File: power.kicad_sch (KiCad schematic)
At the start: 72 parts, among them Q2 PJE138K, Q3 PJE138K, U27 AP62301_TSOT, U28 AP62301_TSOT, U29 SIC431AED-T1-GE3, U30 TPS22976DPUR, U31 TPS22976DPUR

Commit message: [#83736] WIP: Clear ERC
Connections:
- net VCC is gone; now on net +12V_IN: R249.2
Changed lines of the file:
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@@
 	)
 	(junction
+		(at 62.23 72.39)
+		(diameter 0)
+		(color 0 0 0 0)
+	)
+	(junction
 		(at 189.23 77.47)
 		(diameter 0)
@@
 	(wire
 		(pts
-			(xy 59.69 72.39) (xy 104.14 72.39)
+			(xy 59.69 72.39) (xy 62.23 72.39)
 		)
 		(stroke
@@
 	(wire
 		(pts
+			(xy 76.2 48.26) (xy 62.23 48.26)
+		)
+		(stroke
+			(width 0)
+			(type default)
+		)
+	)
+	(wire
+		(pts
 			(xy 165.1 172.72) (xy 165.1 177.8)
 		)
@@
 	(wire
 		(pts
+			(xy 62.23 48.26) (xy 62.23 72.39)
+		)
+		(stroke
+			(width 0)
+			(type default)
+		)
+	)
+	(wire
+		(pts
 			(xy 378.46 200.66) (xy 381 200.66)
 		)
@@
 	(wire
 		(pts
+			(xy 62.23 72.39) (xy 104.14 72.39)
+		)
+		(stroke
+			(width 0)
+			(type default)
+		)
+	)
+	(wire
+		(pts
 			(xy 124.46 238.76) (xy 129.54 238.76)
 		)
@@
 					(unit 1)
 				)
-			)
-		)
-	)
-	(symbol
-		(lib_id "antmicropower:VCC")
-		(at 76.2 48.26 0)
-		(unit 1)
-		(exclude_from_sim no)
-		(in_bom yes)
-		(on_board yes)
-		(dnp no)
-		(property "Reference" "#PWR0255"
-			(at 76.2 52.07 0)
-			(effects
-				(font
-					(size 1.27 1.27)
-				)
-				(justify left bottom)
-				(hide yes)
-			)
-		)
-		(property "Value" "VCC"
-			(at 74.295 44.45 0)
-			(effects
-				(font
-					(size 1.27 1.27)
-				)
-				(justify left)
-			)
-		)
-		(property "Footprint" ""
-			(at 76.2 48.26 0)
-			(effects
-				(font
-					(size 1.27 1.27)
-				)
-				(hide yes)
-			)
-		)
-		(property "Datasheet" ""
-			(at 76.2 48.26 0)
-			(effects
-				(font
-					(size 1.27 1.27)
-				)
-				(hide yes)
-			)
-		)
-		(property "Description" ""
-			(at 76.2 48.26 0)
-			(effects
-				(font
-					(size 1.27 1.27)
-				)
-				(hide yes)
-			)
-		)
-		(pin "1"
-		)
-		(instances
-			(project "bmc-reference-carrier-board"
-				(path "/5f636c45-3c15-4731-8931-4625e0dab7e4/3d29c412-58cb-45c0-928a-e05b1352002d"
-					(reference "#PWR0255")
-					(unit 1)
-				)

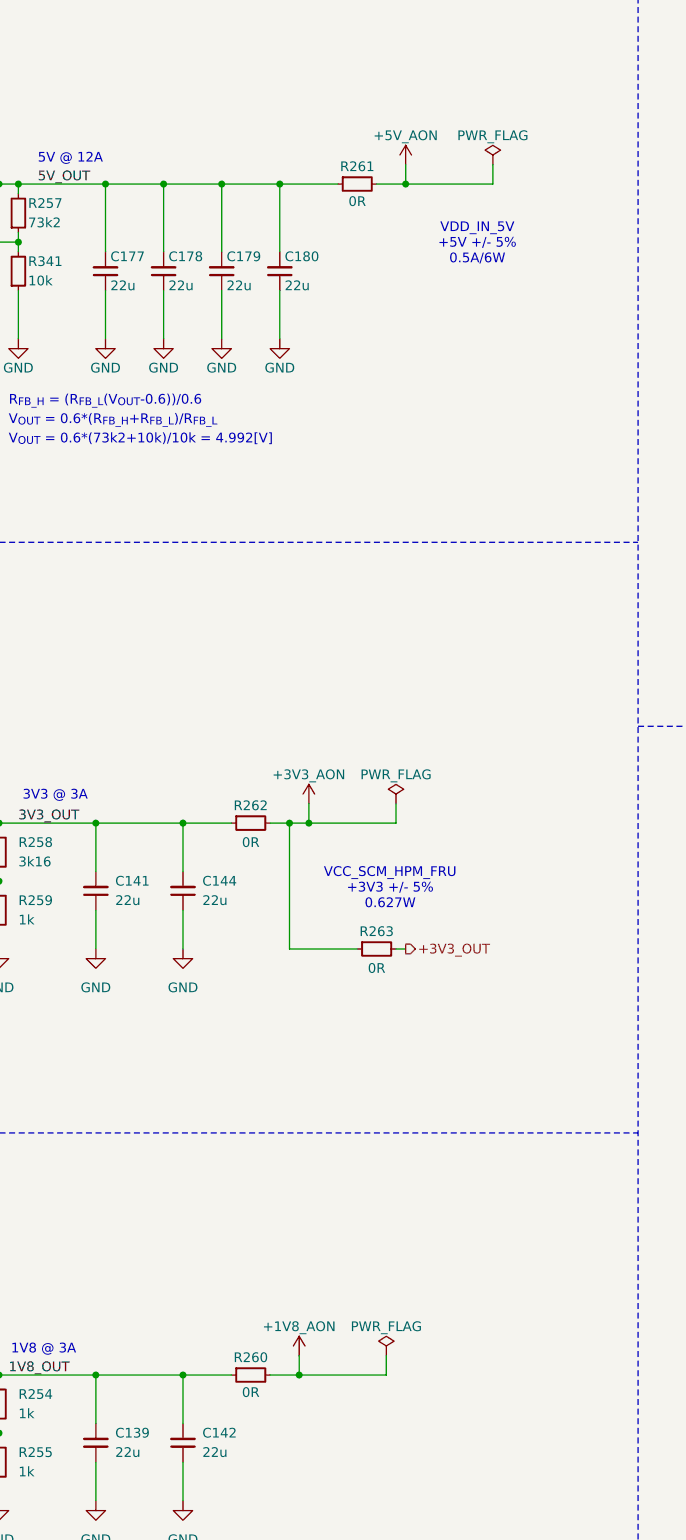
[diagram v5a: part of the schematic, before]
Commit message: [#83767] Layout DC-DC converters, change 0R on power rails to one that can handle more current
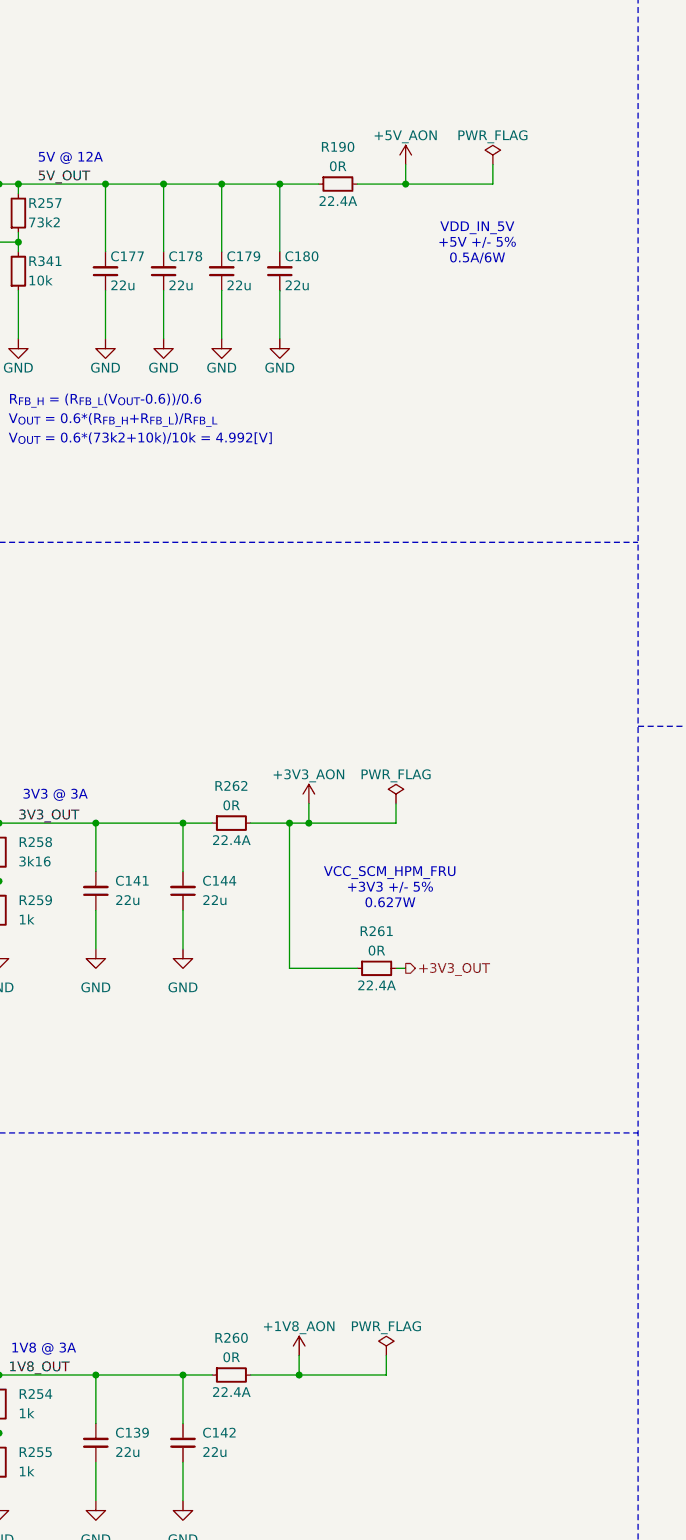
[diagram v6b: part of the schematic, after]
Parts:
- removed R260, R261, R262, R263: R_0R_0402, antmicro-footprints:R_0402_1005Metric, symbol antmicroResistors0402:R_0R_0402
- added R190, R260, R261, R262: R_0R_22.4A_0603, antmicro-footprints:R_0603_1608Metric, symbol antmicroResistors0603:R_0R_22.4A_0603
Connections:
- net +1V8_AON: now also R260.2
- net +3V3_AON: now also R261.1, R262.2
- net +3V3_OUT: now also R261.2
- net +5V_AON: now also R190.2
- net 1V8_OUT: now also R260.1
- net 3V3_OUT: now also R262.1
- net 5V_OUT: now also R190.1

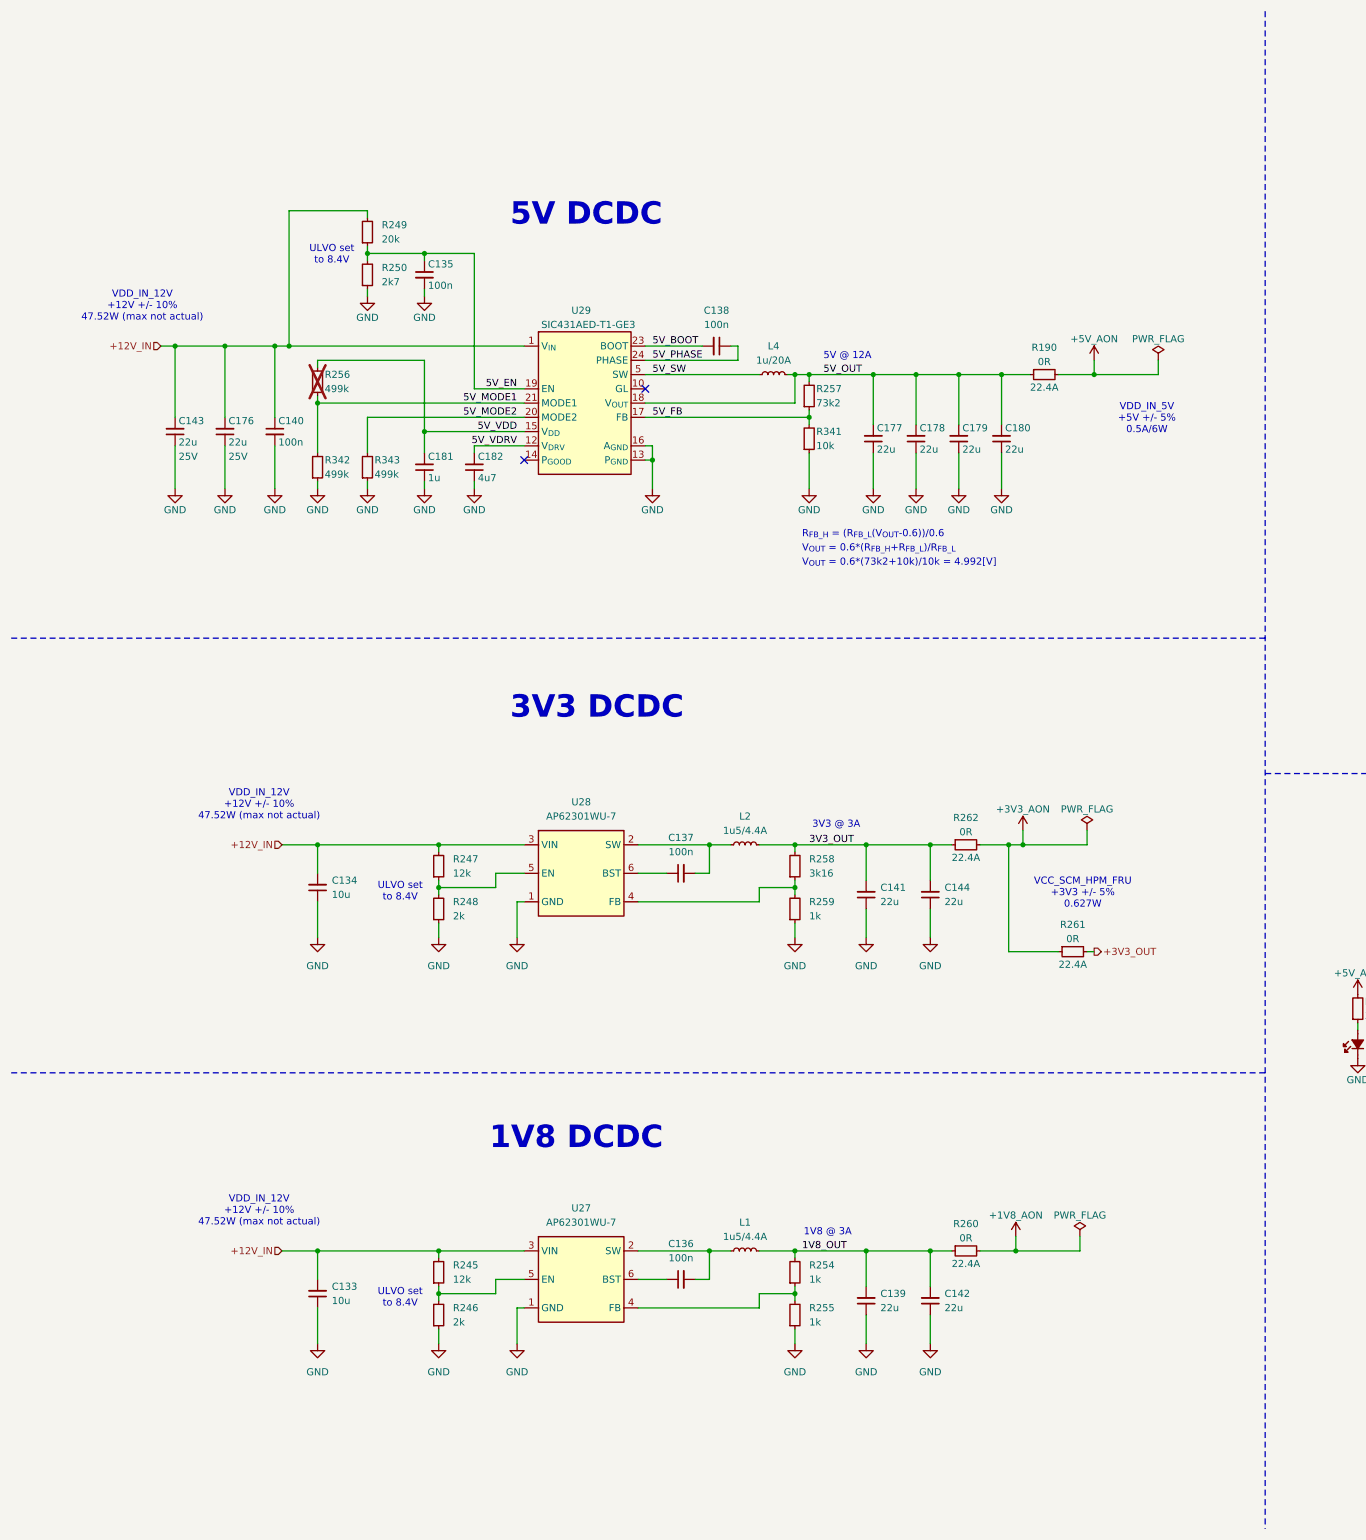
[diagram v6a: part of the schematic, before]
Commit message: [#83904] Add current monitoring IC to the 12V input rail
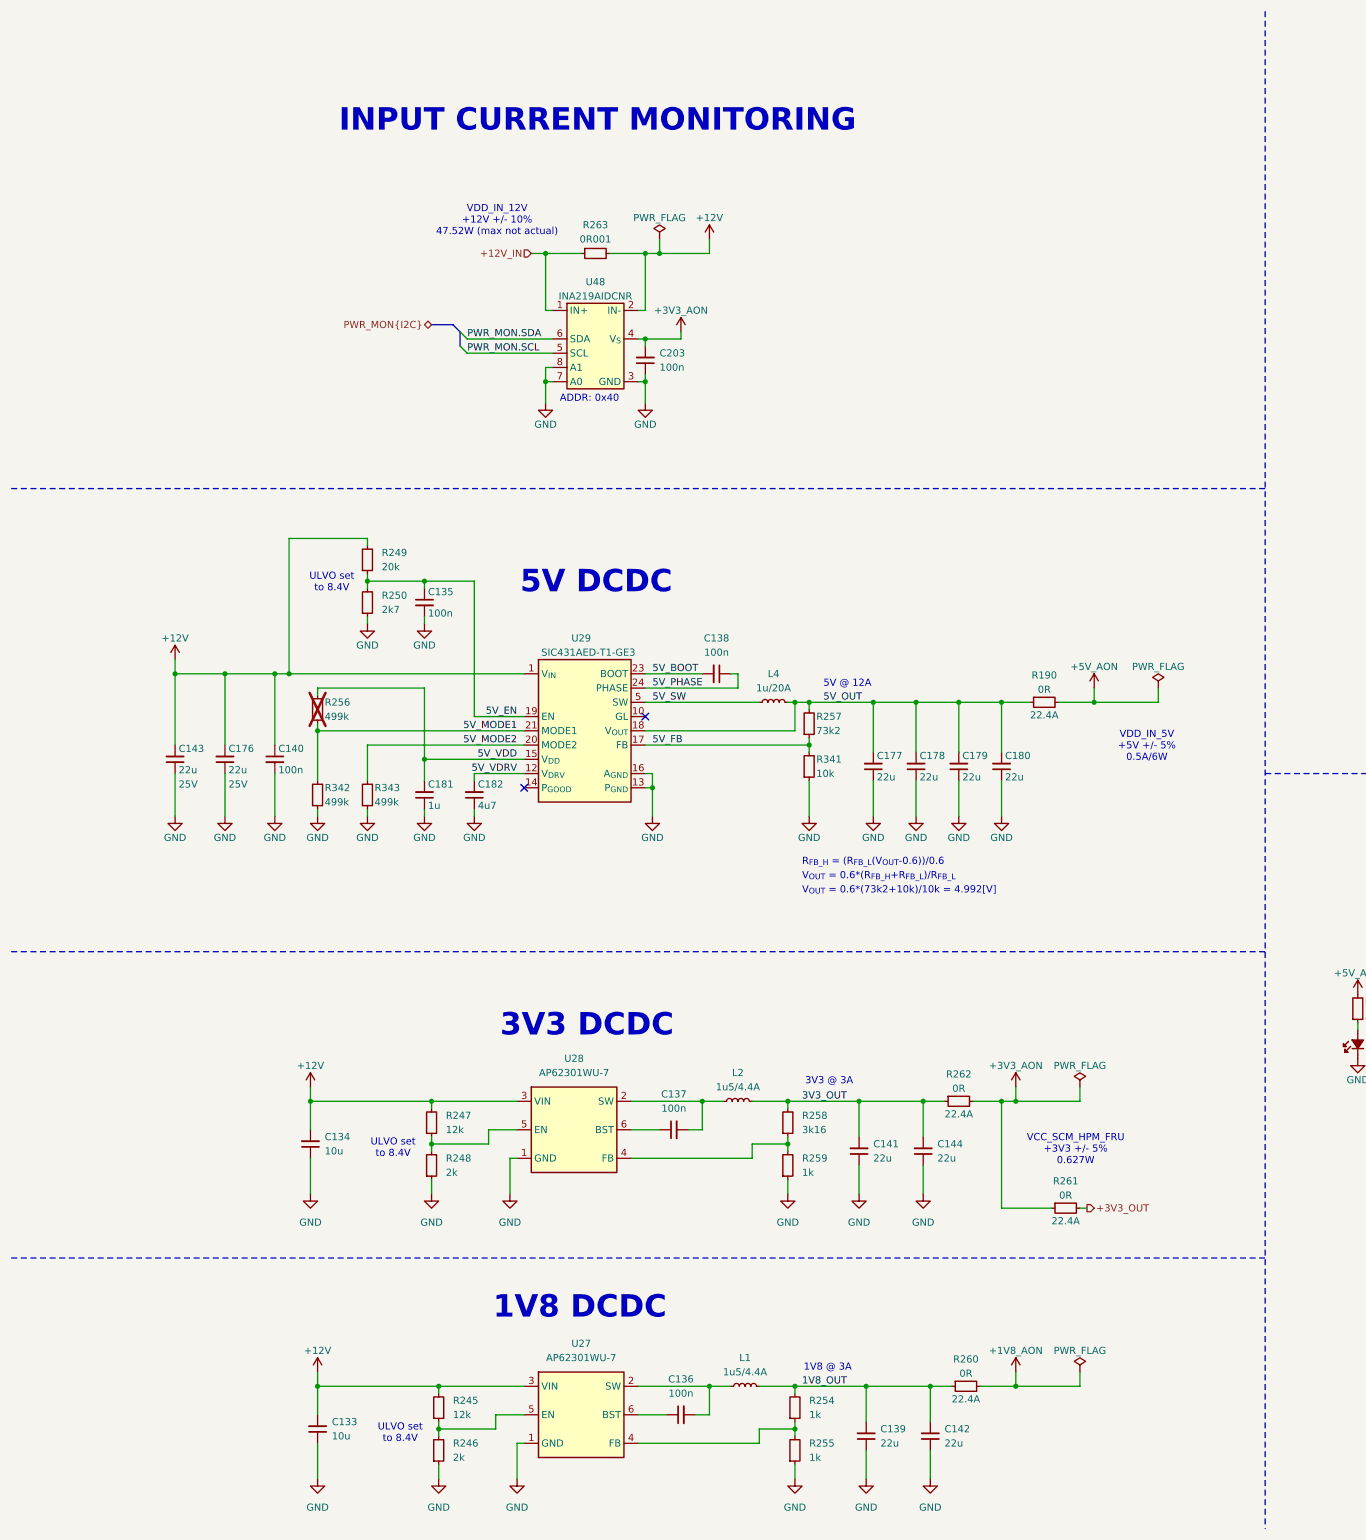
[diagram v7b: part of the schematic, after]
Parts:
- added C203: C_100n_0402, antmicro-footprints:C_0402_1005Metric, symbol antmicroCapacitors0402:C_100n_0402
- added R263: R_0R001_0805, antmicro-footprints:R_0805_2012Metric, symbol antmicroResistorsmisc:R_0R001_0805
- added U48: INA219AIDCNR, antmicro-footprints:SOT-23-8, symbol antmicroPowerMeasurement:INA219AIDCNR
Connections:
- net +12V_IN: now also R263.1, U48.1 (IN+); no longer C133.2, C134.2, C140.1, C143.2, C176.2, R245.2, R247.2, R249.2, U27.3 (VIN), U28.3 (VIN), U29.1 (V_{IN}), U29.2 (V_{IN}), U29.22 (V_{IN}), U29.26 (V_{IN})
- net +3V3_AON: now also C203.2, U48.4 (V_{S})
- net GND: now also C203.1, U48.3 (GND), U48.7 (A0), U48.8 (A1)
- new net +12V: C133.2, C134.2, C140.1, C143.2, C176.2, R245.2, R247.2, R249.2, R263.2, U27.3 (VIN), U28.3 (VIN), U29.1 (V_{IN}), U29.2 (V_{IN}), U29.22 (V_{IN}), U29.26 (V_{IN}), U48.2 (IN-)
- new net PWR_MON.SCL: U48.5 (SCL)
- new net PWR_MON.SDA: U48.6 (SDA)
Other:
- note added: "ADDR: 0x40"
- note added: "INPUT CURRENT MONITORING"
- moved on the sheet: C133, C134, C135, C136, C137, C138, C139, C140, C141, C142, C143, C144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

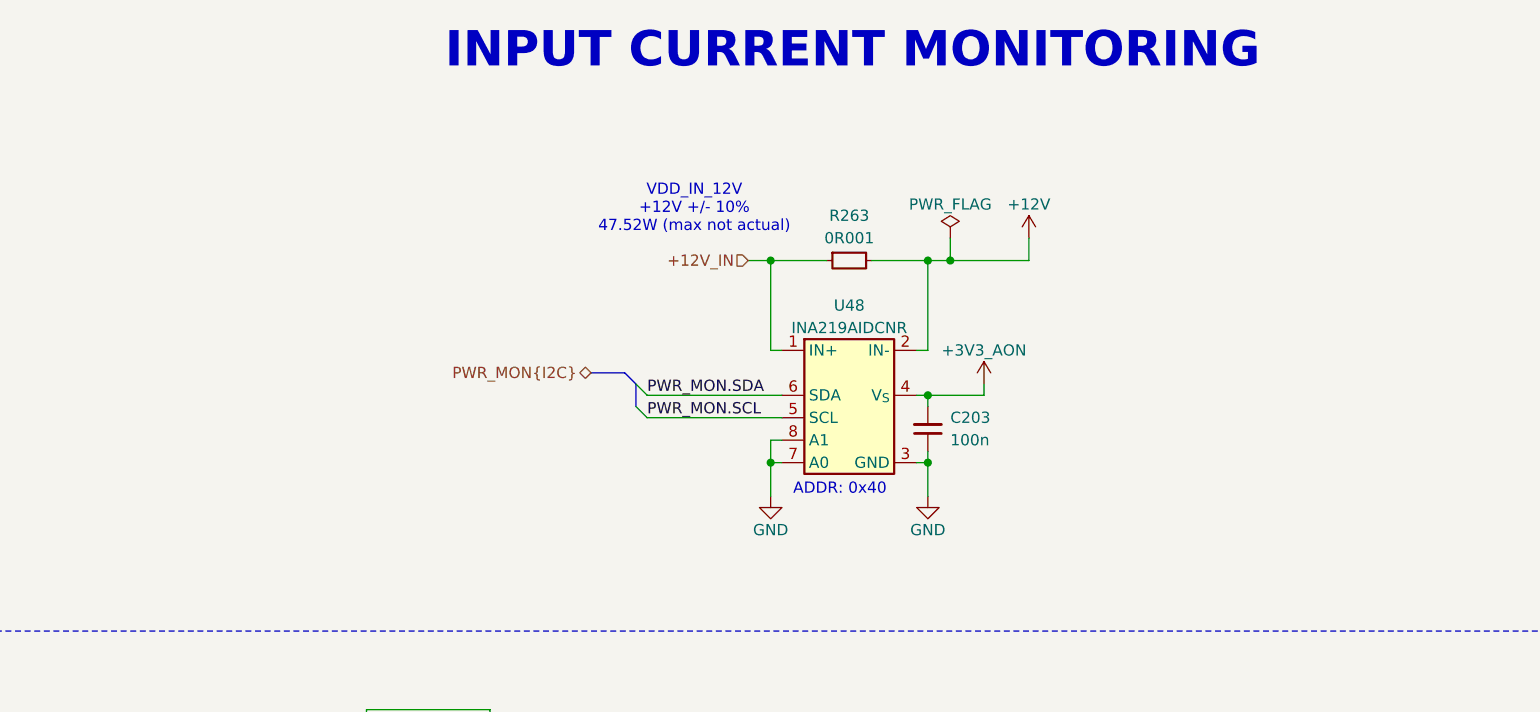
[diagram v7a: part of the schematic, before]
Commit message: [#83904] Add level shifters, clear ERC
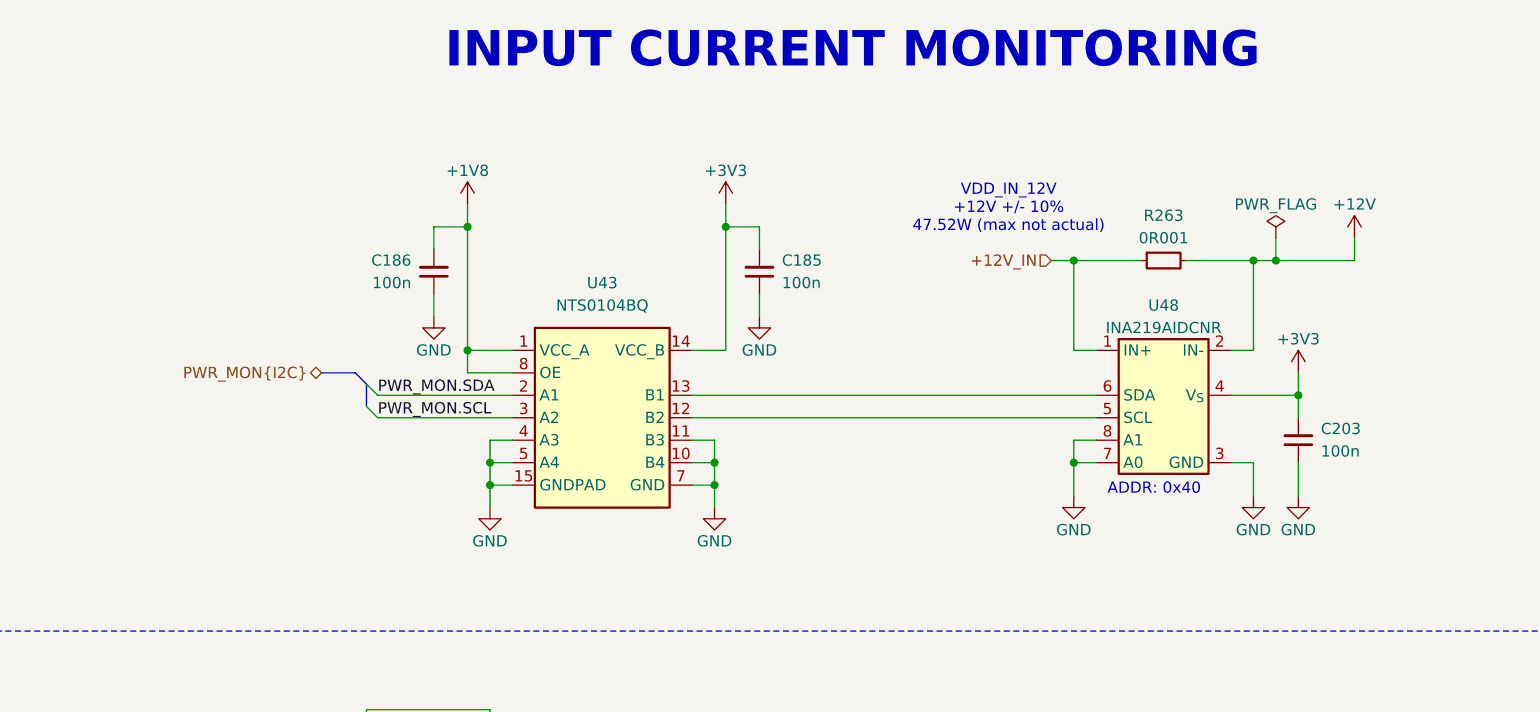
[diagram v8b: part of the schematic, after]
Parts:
- added C185, C186: C_100n_0402, antmicro-footprints:C_0402_1005Metric, symbol antmicroCapacitors0402:C_100n_0402
- added U43: NTS0104_DHVQFN, antmicro-footprints:DHVQFN-14-1EP_2.5x3mm, symbol antmicroLogicTranslatorsLevelShifters:NTS0104_DHVQFN
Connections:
- net +1V8: now also C186.2, U43.1 (VCC_A), U43.8 (OE)
- net +3V3: now also C203.2, U48.4 (V_{S}), C185.2, U43.14 (VCC_B)
- net +3V3_AON: no longer C203.2, U48.4 (V_{S})
- net GND: now also C185.1, C186.1, U43.10 (B4), U43.11 (B3), U43.15 (GNDPAD), U43.4 (A3), U43.5 (A4), U43.7 (GND)
- net PWR_MON.SCL: now also U43.3 (A2); no longer U48.5 (SCL)
- net PWR_MON.SDA: now also U43.2 (A1); no longer U48.6 (SDA)
- new net: U43.12 (B2), U48.5 (SCL)
- new net: U43.13 (B1), U48.6 (SDA)
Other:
- moved on the sheet: C203, R263, U48
